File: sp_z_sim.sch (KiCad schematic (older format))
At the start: 25 parts, among them J1 USB_B_Micro, J2 TEMP1, J3 TEMP1, J4 SWD, J5 OUT1, J6 OUT2, J7 4T_1, J8 4T_2

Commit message: Finished first version of schematic
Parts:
- added C4: 100u, Capacitor_THT:CP_Radial_D10.0mm_P5.00mm, symbol Device:CP_Small
- added C5, C6: 2.2u, Capacitor_SMD:C_1206_3216Metric, symbol Device:C_Small
- added J10: ADC_EXTRA, Connector_JST:JST_PH_B4B-PH-K_1x04_P2.00mm_Vertical, symbol Connector:Conn_01x04_Male
- added J11: IN+, TestPoint:TestPoint_Pad_4.0x4.0mm, symbol Connector:Conn_01x01_Male
- added J12: IN-, TestPoint:TestPoint_Pad_4.0x4.0mm, symbol Connector:Conn_01x01_Male
- C1, C2: footprint (none) -> Capacitor_SMD:C_0603_1608Metric
- C3: renamed from C?; footprint (none) -> Capacitor_SMD:C_0603_1608Metric
- D1, D2: footprint (none) -> LED_SMD:LED_0603_1608Metric
- J1: footprint (none) -> Connector_USB:USB_Micro-B_Molex-105017-0001
- J2, J3: footprint (none) -> Connector_JST:JST_PH_B2B-PH-K_1x02_P2.00mm_Vertical
- J4: footprint (none) -> Connector_JST:JST_PH_B6B-PH-K_1x06_P2.00mm_Vertical
- J6: renamed from J5; footprint (none) -> TestPoint:TestPoint_Pad_4.0x4.0mm
- J7: renamed from J6; footprint (none) -> TestPoint:TestPoint_Pad_4.0x4.0mm
- J8: renamed from J7; footprint (none) -> TestPoint:TestPoint_Pad_4.0x4.0mm
- J9: renamed from J8; footprint (none) -> TestPoint:TestPoint_Pad_4.0x4.0mm
- R1, R2: footprint (none) -> Resistor_SMD:R_0603_1608Metric
- R10, R11, R3, R4, R5, R6, R9: renamed from R?; footprint (none) -> Resistor_SMD:R_0603_1608Metric
- R7: renamed from R3; footprint (none) -> Resistor_SMD:R_0603_1608Metric
- R8: renamed from R4; footprint (none) -> Resistor_SMD:R_0603_1608Metric
- gave numbers to parts that had none: 1
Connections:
- net labels added: PWR_IN
- net labels removed: GNDA
- wire segments 116 -> 138
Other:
- note added: "12061C225KAT2A CAP CER 2.2UF 100V X7R 1206\nC3216X7S2A225K160AB CAP CER 2.2UF 100V X7S 1206\n"
- note added: "Power\nInput"
- note added: "SD Card for logging,\nsample buffering, etc."
- moved on the sheet: C1, C2, C3, D1, D2, J1, J2, J3, J4, J5, J6, J7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

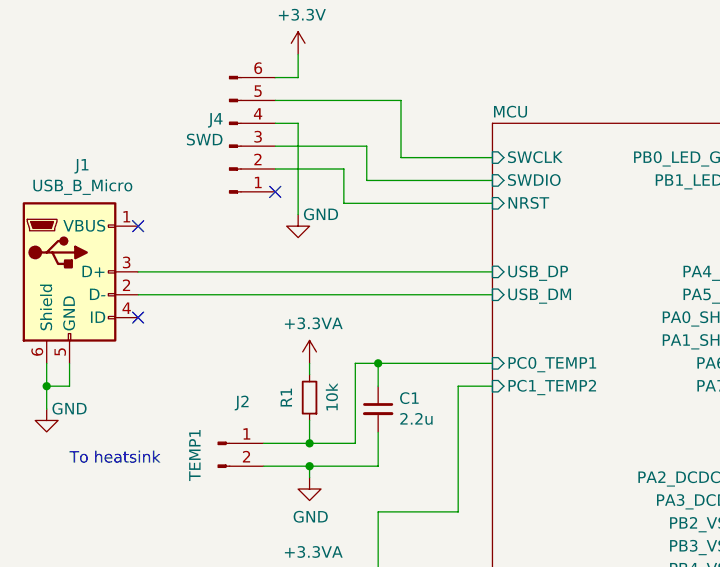
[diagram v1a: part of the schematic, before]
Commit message: preparation for routing and adding kylfläns
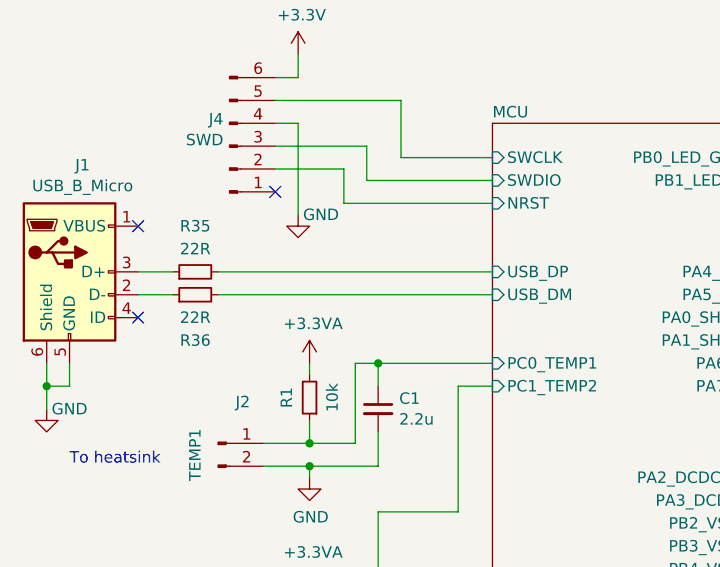
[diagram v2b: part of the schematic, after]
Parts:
- added R35, R36: 22R, Resistor_SMD:R_0603_1608Metric, symbol Device:R_Small
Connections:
- net MCU/USB_DM: now also R36.2; no longer J1.2 (D-)
- net MCU/USB_DP: now also R35.2; no longer J1.3 (D+)
- new net: J1.2 (D-), R36.1
- new net: J1.3 (D+), R35.1
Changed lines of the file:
@@
 	1    0    0    -1
 $EndComp
-Wire Wire Line
-	3100 1950 1550 1950
-Wire Wire Line
-	1550 2050 3100 2050
 $Comp
 L power:GND #PWR01
@@
 Text Notes 7300 4900 0    50   ~ 0
 SD Card for logging,\nsample buffering, etc.
+$Comp
+L Device:R_Small R35
+U 1 1 5DB9CDE0
+P 1800 1950
+F 0 "R35" V 2000 1950 50  0000 C CNN
+F 1 "22R" V 1900 1950 50  0000 C CNN
+F 2 "Resistor_SMD:R_0603_1608Metric" H 1800 1950 50  0001 C CNN
+F 3 "~" H 1800 1950 50  0001 C CNN
+	1    1800 1950
+	0    -1   -1   0
+$EndComp
+$Comp
+L Device:R_Small R36
+U 1 1 5DB9E98E
+P 1800 2050
+F 0 "R36" V 1600 2050 50  0000 C CNN
+F 1 "22R" V 1700 2050 50  0000 C CNN
+F 2 "Resistor_SMD:R_0603_1608Metric" H 1800 2050 50  0001 C CNN
+F 3 "~" H 1800 2050 50  0001 C CNN
+	1    1800 2050
+	0    -1   -1   0
+$EndComp
+Wire Wire Line
+	1550 1950 1700 1950
+Wire Wire Line
+	1700 2050 1550 2050
+Wire Wire Line
+	1900 1950 3100 1950
+Wire Wire Line
+	3100 2050 1900 2050
 $EndSCHEMATC

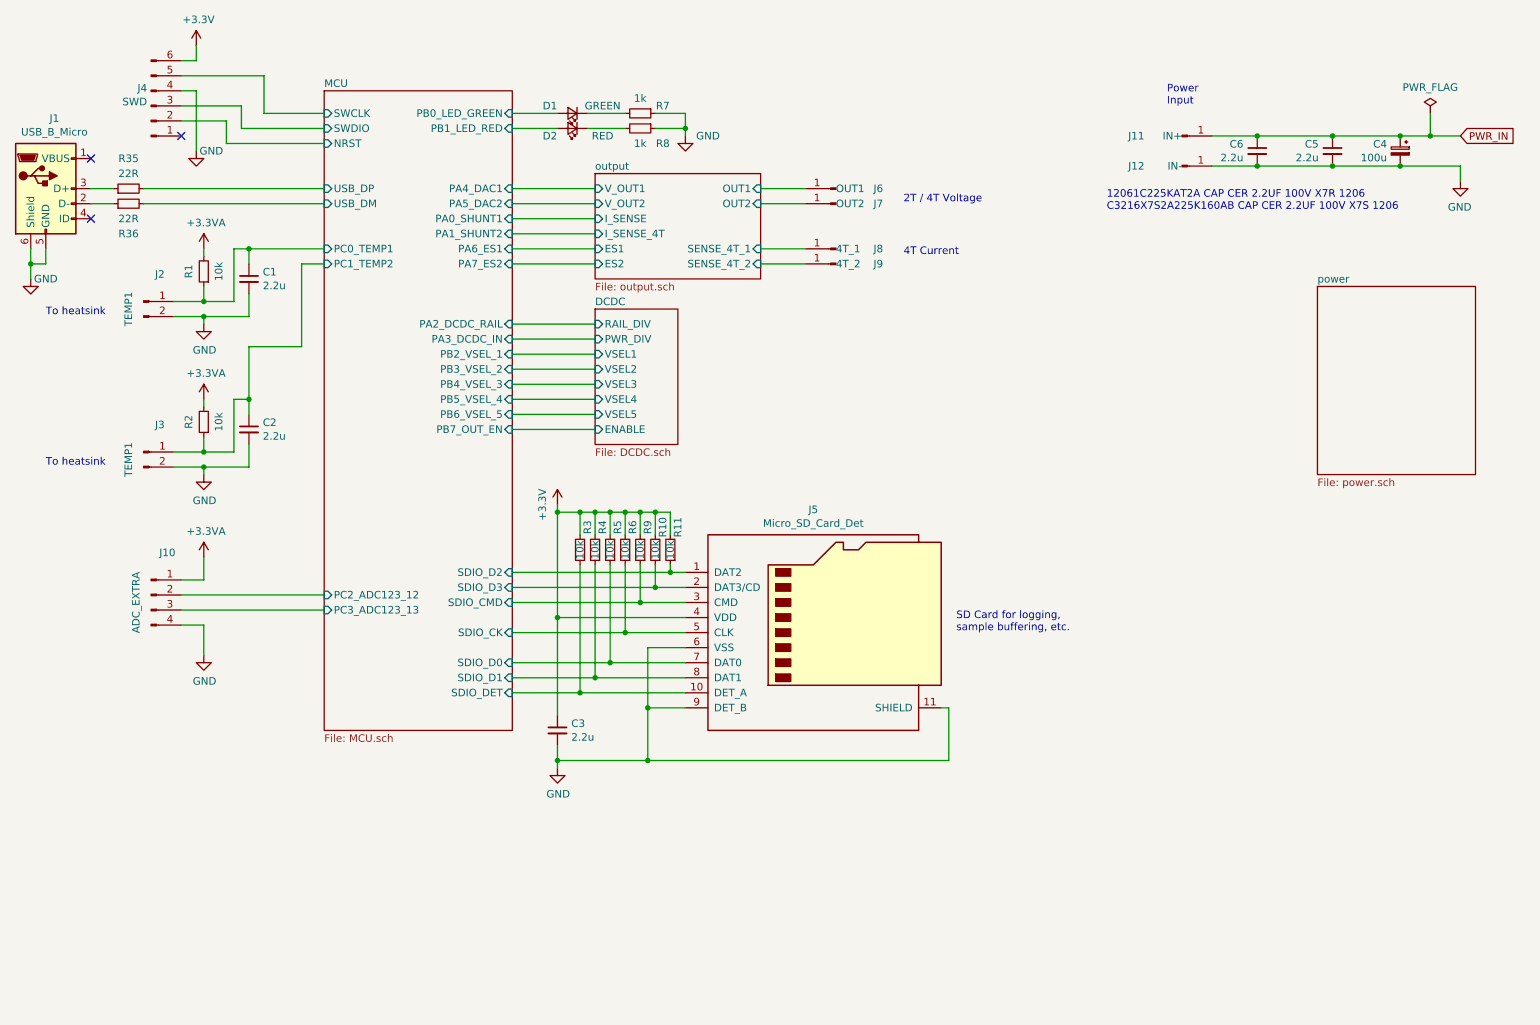
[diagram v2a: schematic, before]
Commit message: Schematic updates, added 3D models and started routing
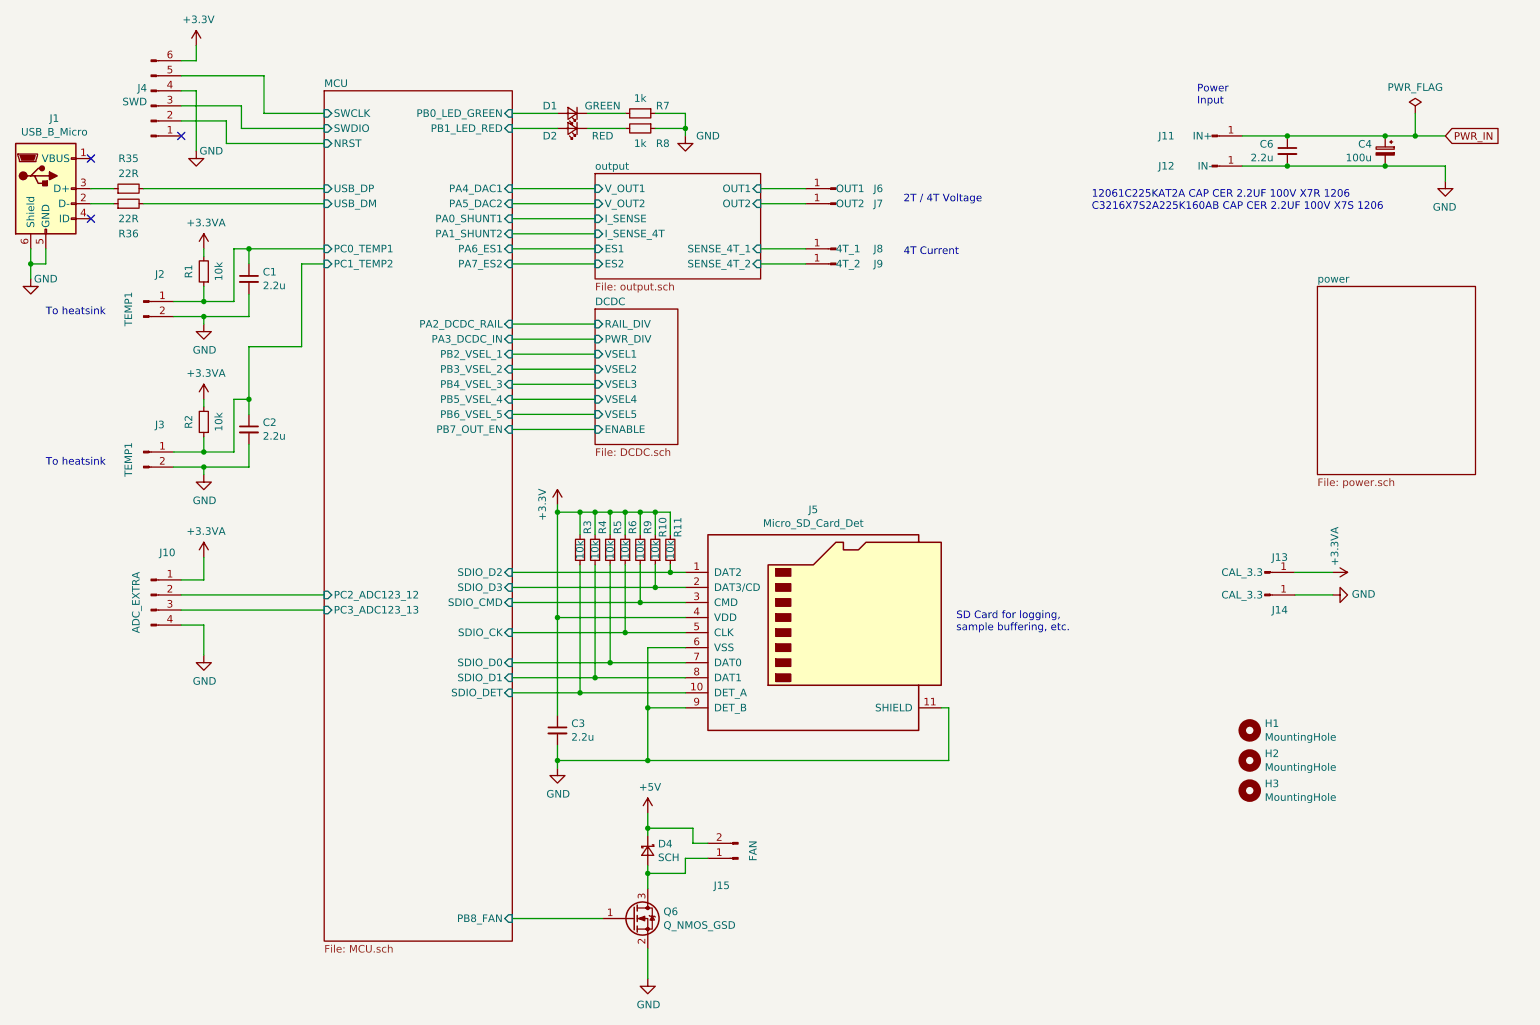
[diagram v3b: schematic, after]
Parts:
- removed C5: 2.2u, Capacitor_SMD:C_1206_3216Metric, symbol Device:C_Small
- added D4: SCH, Diode_SMD:D_SMA, symbol Device:D_Schottky_Small
- added H1, H2, H3: MountingHole, MountingHole:MountingHole_3.2mm_M3, symbol Mechanical:MountingHole
- added J13, J14: CAL_3.3, TestPoint:TestPoint_Pad_3.0x3.0mm, symbol Connector:Conn_01x01_Male
- added J15: FAN, Connector_JST:JST_PH_B2B-PH-K_1x02_P2.00mm_Vertical, symbol Connector:Conn_01x02_Male
- added Q6: Q_NMOS_GSD, Package_TO_SOT_SMD:SOT-23, symbol Device:Q_NMOS_GSD
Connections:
- net +3.3VA: now also J13.1 (Pin_1)
- net GND: now also J14.1 (Pin_1), Q6.2 (S)
- new net: D4.2 (A), J15.1 (Pin_1), Q6.3 (D)
- new net +5V: D4.1 (K), J15.2 (Pin_2)
- new net MCU/PB8_FAN: Q6.1 (G)
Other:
- moved on the sheet: C4, C6, J11, J12

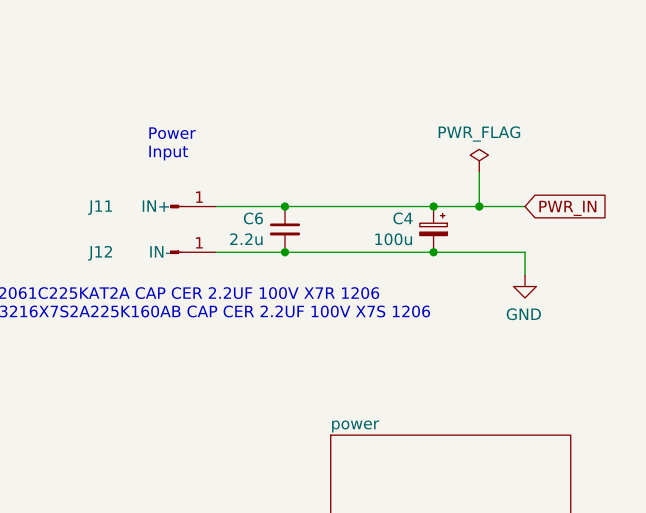
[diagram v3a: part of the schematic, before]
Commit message: Finished routing and added some 3D models
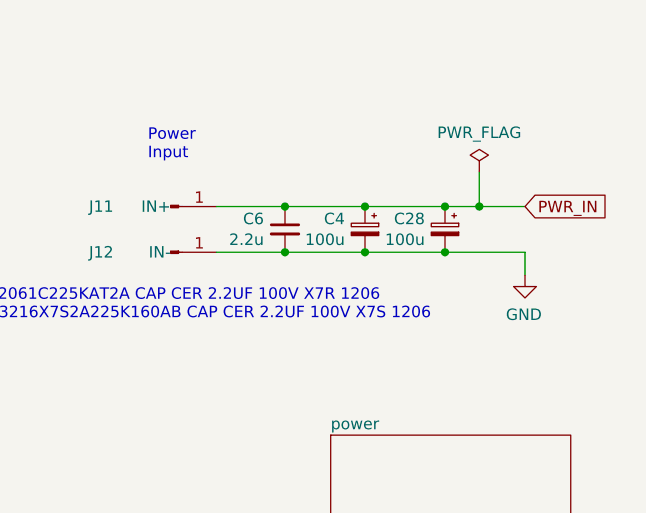
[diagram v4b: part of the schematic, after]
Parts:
- added C28: 100u, Capacitor_THT:CP_Radial_D10.0mm_P5.00mm, symbol Device:CP_Small
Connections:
- net GND: now also C28.2
- net PWR_IN: now also C28.1
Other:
- moved on the sheet: C4
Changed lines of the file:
@@
 L Device:CP_Small C4
 U 1 1 5D9EE9D3
-P 10150 1700
-F 0 "C4" H 10238 1746 50  0000 L CNN
-F 1 "100u" H 10238 1655 50  0000 L CNN
-F 2 "Capacitor_THT:CP_Radial_D10.0mm_P5.00mm" H 10150 1700 50  0001 C CNN
-F 3 "~" H 10150 1700 50  0001 C CNN
-F 4 "https://www.digikey.se/product-detail/en/nichicon/URS1J101MPD1TD/493-11829-1-ND/4320229" H 10150 1700 50  0001 C CNN "digikey"
-	1    10150 1700
+P 9850 1700
+F 0 "C4" H 9938 1746 50  0000 L CNN
+F 1 "100u" H 9938 1655 50  0000 L CNN
+F 2 "Capacitor_THT:CP_Radial_D10.0mm_P5.00mm" H 9850 1700 50  0001 C CNN
+F 3 "~" H 9850 1700 50  0001 C CNN
+F 4 "https://www.digikey.se/product-detail/en/nichicon/URS1J101MPD1TD/493-11829-1-ND/4320229" H 9850 1700 50  0001 C CNN "digikey"
+	1    9850 1700
 	-1   0    0    -1
 $EndComp
-Connection ~ 10150 1800
-Connection ~ 10150 1600
+Connection ~ 9850 1800
+Connection ~ 9850 1600
 $Comp
 L power:GND #PWR013
@@
 	10550 1600 10350 1600
 Wire Wire Line
-	10550 1800 10150 1800
+	10550 1800 10200 1800
 $Comp
 L power:+3.3VA #PWR0102
@@
 Connection ~ 10350 1600
 Wire Wire Line
-	10350 1600 10150 1600
+	10350 1600 10200 1600
 Text Notes 7300 4900 0    50   ~ 0
 SD Card for logging,\nsample buffering, etc.
@@
 	3100 2050 1900 2050
 Wire Wire Line
-	9500 1600 10150 1600
-Wire Wire Line
-	9500 1800 10150 1800
+	9500 1600 9850 1600
+Wire Wire Line
+	9500 1800 9850 1800
 $Comp
 L power:+3.3VA #PWR036
@@
 	1    0    0    -1
 $EndComp
+$Comp
+L Device:CP_Small C28
+U 1 1 5DC02D42
+P 10200 1700
+F 0 "C28" H 10288 1746 50  0000 L CNN
+F 1 "100u" H 10288 1655 50  0000 L CNN
+F 2 "Capacitor_THT:CP_Radial_D10.0mm_P5.00mm" H 10200 1700 50  0001 C CNN
+F 3 "~" H 10200 1700 50  0001 C CNN
+F 4 "https://www.digikey.se/product-detail/en/nichicon/URS1J101MPD1TD/493-11829-1-ND/4320229" H 10200 1700 50  0001 C CNN "digikey"
+	1    10200 1700
+	-1   0    0    -1
+$EndComp
+Connection ~ 10200 1600
+Wire Wire Line
+	10200 1600 9850 1600
+Connection ~ 10200 1800
+Wire Wire Line
+	10200 1800 9850 1800
 $EndSCHEMATC
